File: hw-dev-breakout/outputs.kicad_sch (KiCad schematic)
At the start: 47 parts, among them J301 WAGO 250-220, J302 Conn_01x20, Q301 2N7002, Q302 2N7002, Q303 2N7002, Q304 2N7002, Q305 2N7002, Q306 2N7002, Q307 2N7002, Q308 HL 20N04, Q309 HL 20N04, Q310 2N7002, Q311 Q_PMOS_HL_4485

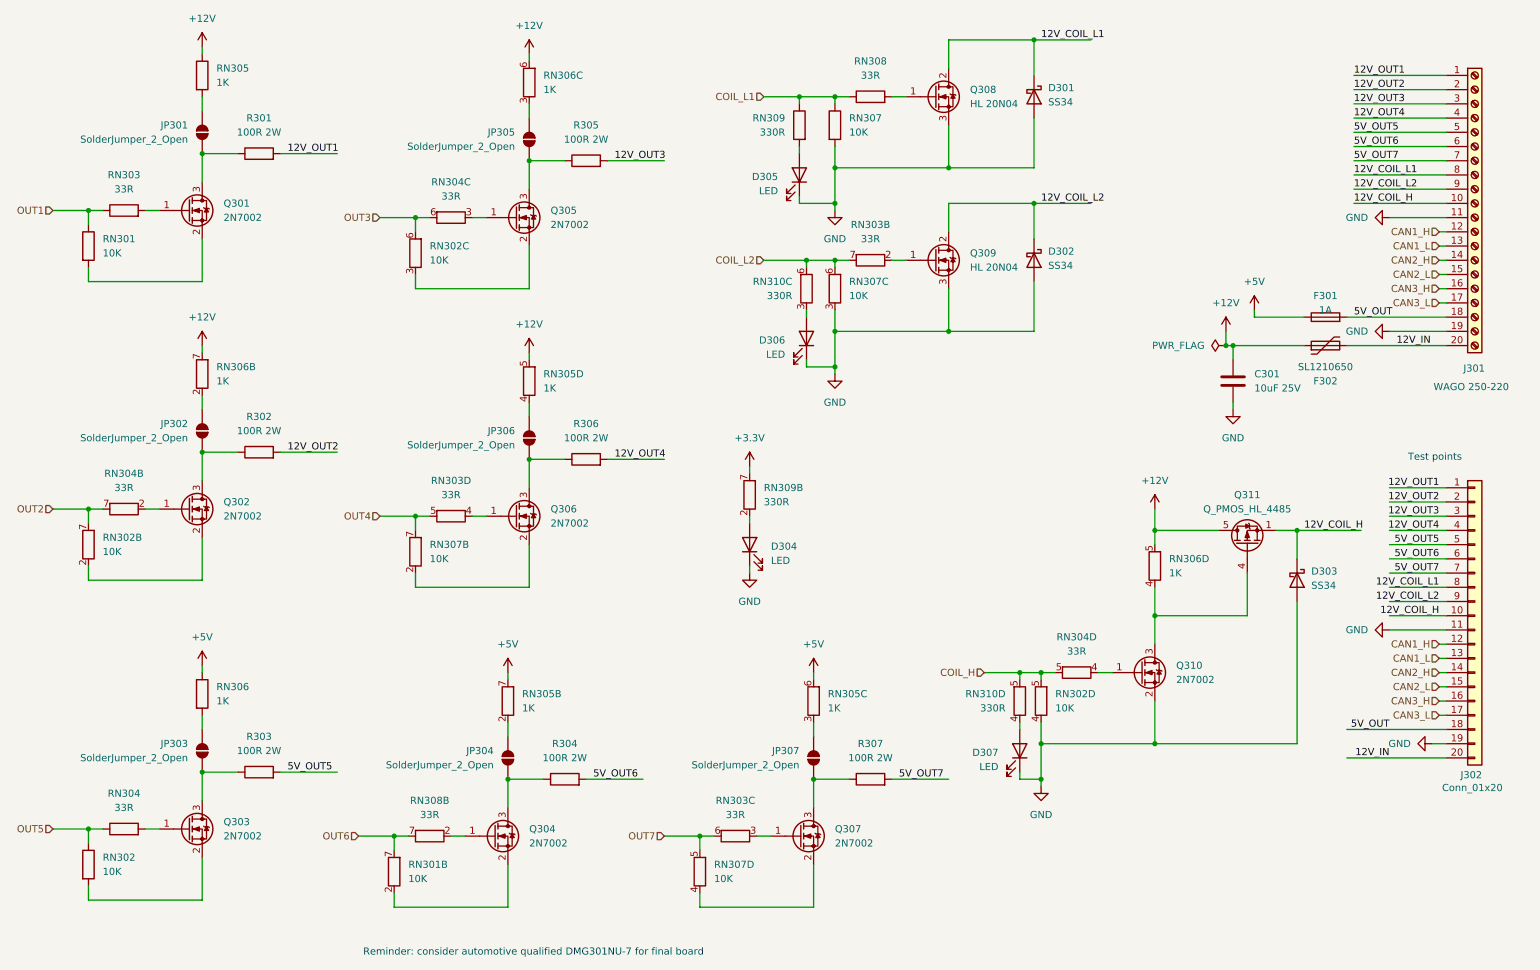
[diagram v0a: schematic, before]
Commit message: Complete schematic with footprint assignments
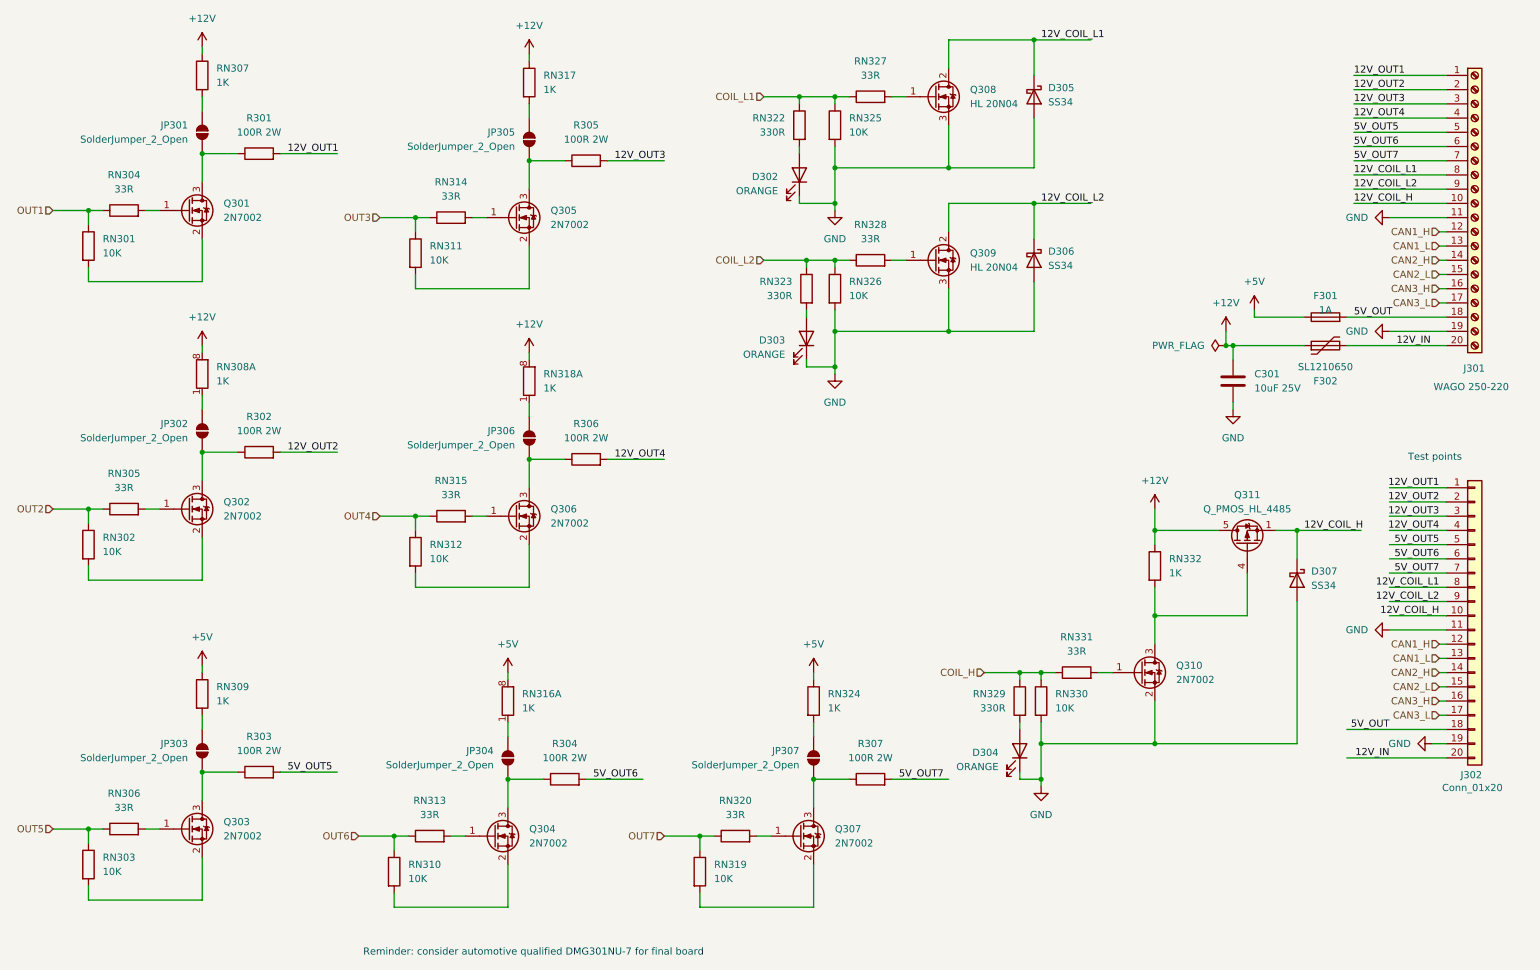
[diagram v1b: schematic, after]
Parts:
- removed D304: LED, symbol Device:LED
- removed unit 2 of RN309
- D302: renamed from D305; value LED -> ORANGE; footprint (none) -> LED_SMD:LED_0603_1608Metric
- D303: renamed from D306; value LED -> ORANGE; footprint (none) -> LED_SMD:LED_0603_1608Metric
- D304: renamed from D307; value LED -> ORANGE; footprint (none) -> LED_SMD:LED_0603_1608Metric
- J301: footprint (none) -> hw-dev-breakout:CONN-TH_250-220
- J302: footprint (none) -> Connector_PinHeader_2.54mm:PinHeader_1x01_P2.54mm_Vertical
- R301, R302, R303, R304, R305, R306, R307: footprint Resistor_SMD:R_Array_Convex_4x0603 -> Resistor_SMD:R_2512_6332Metric
- RN301: footprint Resistor_SMD:R_Array_Convex_4x0603 -> Resistor_SMD:R_0603_1608Metric
- RN302: footprint Resistor_SMD:R_Array_Convex_4x0603 -> Resistor_SMD:R_0603_1608Metric; symbol Device:R_Pack04_Split -> Device:R
- RN303: renamed from RN302; footprint Resistor_SMD:R_Array_Convex_4x0603 -> Resistor_SMD:R_0603_1608Metric
- RN304: renamed from RN303; footprint Resistor_SMD:R_Array_Convex_4x0603 -> Resistor_SMD:R_0603_1608Metric
- RN305, RN314, RN331: renamed from RN304; footprint Resistor_SMD:R_Array_Convex_4x0603 -> Resistor_SMD:R_0603_1608Metric; symbol Device:R_Pack04_Split -> Device:R
- RN306: renamed from RN304; footprint Resistor_SMD:R_Array_Convex_4x0603 -> Resistor_SMD:R_0603_1608Metric
- RN307, RN316, RN318: renamed from RN305; footprint Resistor_SMD:R_Array_Convex_4x0603 -> Resistor_SMD:R_0603_1608Metric
- RN308, RN309: renamed from RN306; footprint Resistor_SMD:R_Array_Convex_4x0603 -> Resistor_SMD:R_0603_1608Metric
- RN310: renamed from RN301; footprint Resistor_SMD:R_Array_Convex_4x0603 -> Resistor_SMD:R_0603_1608Metric; symbol Device:R_Pack04_Split -> Device:R
- RN311, RN330: renamed from RN302; footprint Resistor_SMD:R_Array_Convex_4x0603 -> Resistor_SMD:R_0603_1608Metric; symbol Device:R_Pack04_Split -> Device:R
- RN312, RN319, RN326: renamed from RN307; footprint Resistor_SMD:R_Array_Convex_4x0603 -> Resistor_SMD:R_0603_1608Metric; symbol Device:R_Pack04_Split -> Device:R
- RN313: renamed from RN308; footprint Resistor_SMD:R_Array_Convex_4x0603 -> Resistor_SMD:R_0603_1608Metric; symbol Device:R_Pack04_Split -> Device:R
- RN315, RN320, RN328: renamed from RN303; footprint Resistor_SMD:R_Array_Convex_4x0603 -> Resistor_SMD:R_0603_1608Metric; symbol Device:R_Pack04_Split -> Device:R
- RN317, RN332: renamed from RN306; footprint Resistor_SMD:R_Array_Convex_4x0603 -> Resistor_SMD:R_0603_1608Metric; symbol Device:R_Pack04_Split -> Device:R
- RN322: renamed from RN309; footprint (none) -> Resistor_SMD:R_0603_1608Metric
- RN323, RN329: renamed from RN310; footprint (none) -> Resistor_SMD:R_0603_1608Metric; symbol Device:R_Pack04_Split -> Device:R
- RN324: renamed from RN305; footprint Resistor_SMD:R_Array_Convex_4x0603 -> Resistor_SMD:R_0603_1608Metric; symbol Device:R_Pack04_Split -> Device:R
- RN325: renamed from RN307; footprint Resistor_SMD:R_Array_Convex_4x0603 -> Resistor_SMD:R_0603_1608Metric
- RN327: renamed from RN308; footprint Resistor_SMD:R_Array_Convex_4x0603 -> Resistor_SMD:R_0603_1608Metric
- renumbered D301 to D305, D302 to D306, D303 to D307
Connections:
- net +12V: now also RN308.8 (R1.2), RN317.1, RN318.8 (R1.2), RN332.1; no longer RN308.7 (R2.2), RN317.6 (R3.2), RN318.5 (R4.2), RN332.5 (R4.2)
- net +5V: now also RN316.8 (R1.2), RN324.1; no longer RN316.7 (R2.2), RN324.6 (R3.2)
- net COIL_H: now also RN329.1, RN330.1, RN331.1; no longer RN329.5 (R4.2), RN330.5 (R4.2), RN331.5 (R4.2)
- net COIL_L2: now also RN323.1, RN326.1, RN328.1; no longer RN323.6 (R3.2), RN326.6 (R3.2), RN328.7 (R2.2)
- net GND: now also RN326.2, RN330.2; no longer RN326.3 (R3.1), RN330.4 (R4.1)
- net OUT2: now also RN302.1, RN305.1; no longer RN302.7 (R2.2), RN305.7 (R2.2)
- net OUT3: now also RN311.1, RN314.1; no longer RN311.6 (R3.2), RN314.6 (R3.2)
- net OUT4: now also RN312.1, RN315.1; no longer RN312.7 (R2.2), RN315.5 (R4.2)
- net OUT6: now also RN310.1, RN313.1; no longer RN310.7 (R2.2), RN313.7 (R2.2)
- net OUT7: now also RN319.1, RN320.1; no longer RN319.5 (R4.2), RN320.6 (R3.2)
- net at D304.2 (A): now also RN329.2; no longer RN329.4 (R4.1)
- net at JP306.1 (A): now also RN318.1 (R1.1); no longer RN318.4 (R4.1)
- net at Q305.2 (S): now also RN311.2; no longer RN311.3 (R3.1)
- net at Q306.1 (G): now also RN315.2; no longer RN315.4 (R4.1)
- net at D303.2 (A): now also RN323.2; no longer RN323.3 (R3.1)
- net at Q307.1 (G): now also RN320.2; no longer RN320.3 (R3.1)
- net at Q307.2 (S): now also RN319.2; no longer RN319.4 (R4.1)
- net at Q310.3 (D), Q311.4 (G): now also RN332.2; no longer RN332.4 (R4.1)
- net at JP307.1 (A): now also RN324.2; no longer RN324.3 (R3.1)
- net at JP304.1 (A): now also RN316.1 (R1.1); no longer RN316.2 (R2.1)
- net at JP302.1 (A): now also RN308.1 (R1.1); no longer RN308.2 (R2.1)
- net at Q310.1 (G): now also RN331.2; no longer RN331.4 (R4.1)
- net at Q305.1 (G): now also RN314.2; no longer RN314.3 (R3.1)
- net at JP305.1 (A): now also RN317.2; no longer RN317.3 (R3.1)

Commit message: pcb: Initial components placed
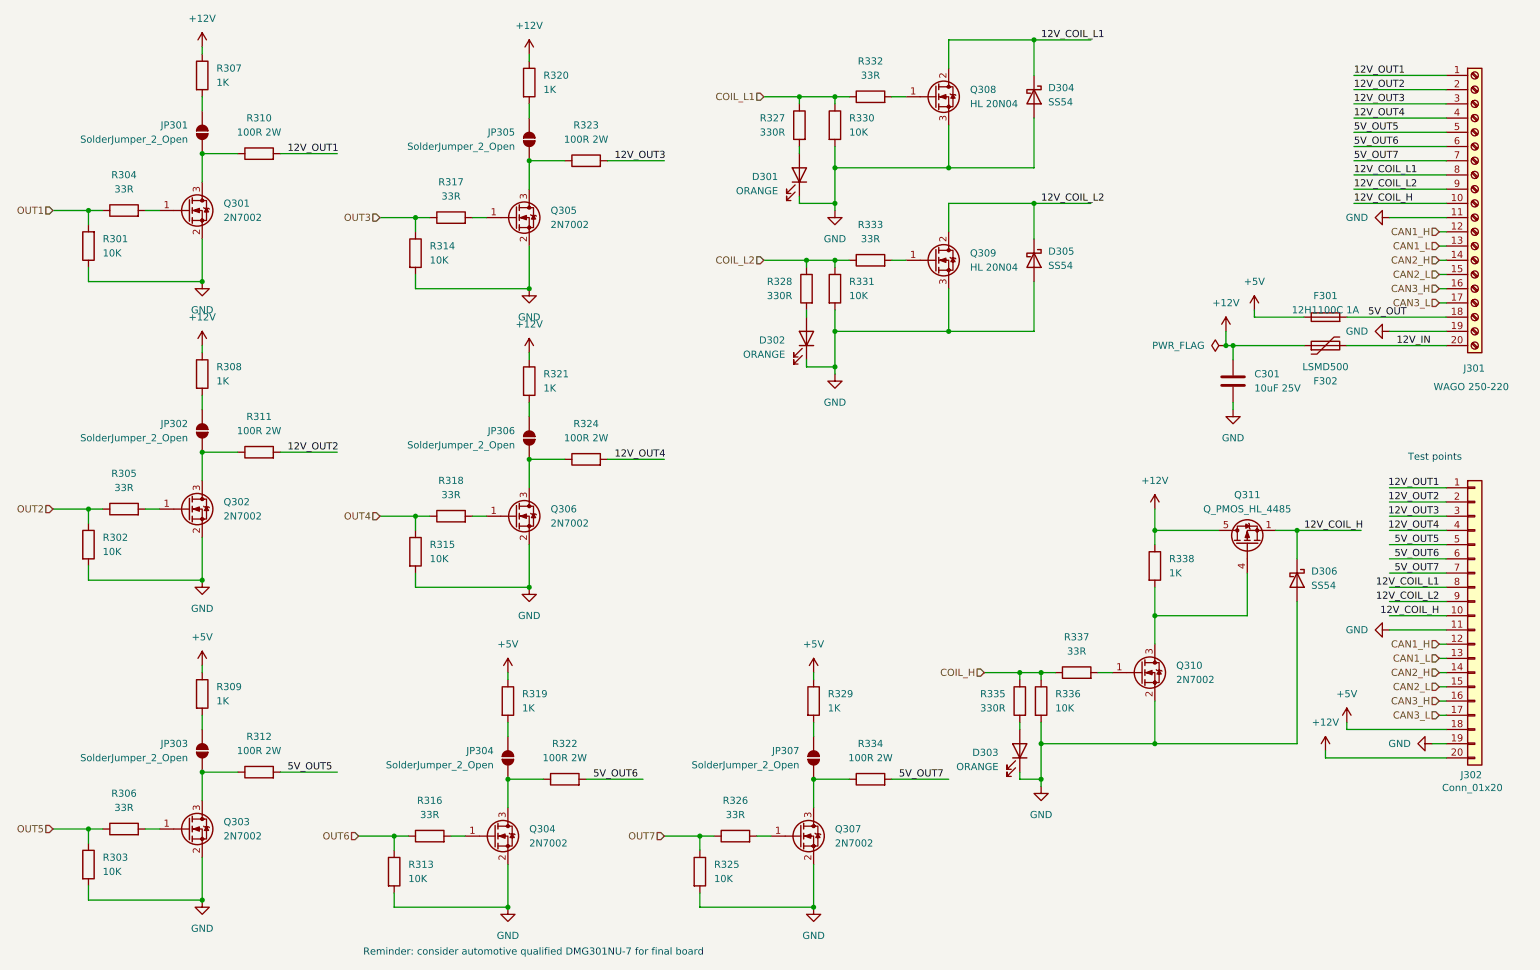
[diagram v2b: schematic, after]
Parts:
- removed RN301: 10K, Resistor_SMD:R_0603_1608Metric, symbol Device:R
- added R301: 10K, Resistor_SMD:R_0603_1608Metric, symbol Device:R
- D304: renamed from D305; value SS34 -> SS54
- D305: renamed from D306; value SS34 -> SS54
- D306: renamed from D307; value SS34 -> SS54
- F301: value 1A -> 12H1100C 1A; footprint Fuse:Fuse_1210_3225Metric -> Fuse:Fuse_1206_3216Metric
- F302: value SL1210650 -> LSMD500; footprint Fuse:Fuse_1210_3225Metric -> Fuse:Fuse_2920_7451Metric
- J302: footprint Connector_PinHeader_2.54mm:PinHeader_1x01_P2.54mm_Vertical -> Connector_PinSocket_2.54mm:PinSocket_1x20_P2.54mm_Vertical
- Q308, Q309: footprint Package_TO_SOT_SMD:TO-252-2 -> Package_TO_SOT_SMD:TO-252-3_TabPin2
- R308: renamed from RN308; symbol Device:R_Pack04_Split -> Device:R
- R319: renamed from RN316; symbol Device:R_Pack04_Split -> Device:R
- R321: renamed from RN318; symbol Device:R_Pack04_Split -> Device:R
- renumbered D302 to D301, D303 to D302, D304 to D303, RN302 to R302, RN303 to R303, RN304 to R304, RN305 to R305, RN306 to R306, RN307 to R307, RN309 to R309, R301 to R310, R302 to R311, R303 to R312, RN310 to R313, RN311 to R314, RN312 to R315, RN313 to R316, RN314 to R317, RN315 to R318, RN317 to R320, R304 to R322, R305 to R323, R306 to R324, RN319 to R325, RN320 to R326, RN322 to R327, RN323 to R328, RN324 to R329, RN325 to R330, RN326 to R331, RN327 to R332, RN328 to R333, R307 to R334, RN329 to R335, RN330 to R336, RN331 to R337, RN332 to R338
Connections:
- net +12V: now also J302.20 (Pin_20), R308.1, R321.1; no longer R308.8 (R1.2), R321.8 (R1.2)
- net +5V: now also J302.18 (Pin_18), R319.1; no longer R319.8 (R1.2)
- net 12V_IN: no longer J302.20 (Pin_20)
- net 5V_OUT: no longer J302.18 (Pin_18)
- net GND: now also Q301.2 (S), Q302.2 (S), Q303.2 (S), Q304.2 (S), Q305.2 (S), Q306.2 (S), Q307.2 (S), R302.2, R303.2, R313.2, R314.2, R315.2, R325.2, R301.1
- net OUT1: now also R301.2
- net at JP306.1 (A): now also R321.2; no longer R321.1 (R1.1)
- net at JP304.1 (A): now also R319.2; no longer R319.1 (R1.1)
- net at JP302.1 (A): now also R308.2; no longer R308.1 (R1.1)
